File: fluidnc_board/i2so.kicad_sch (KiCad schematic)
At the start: 13 parts

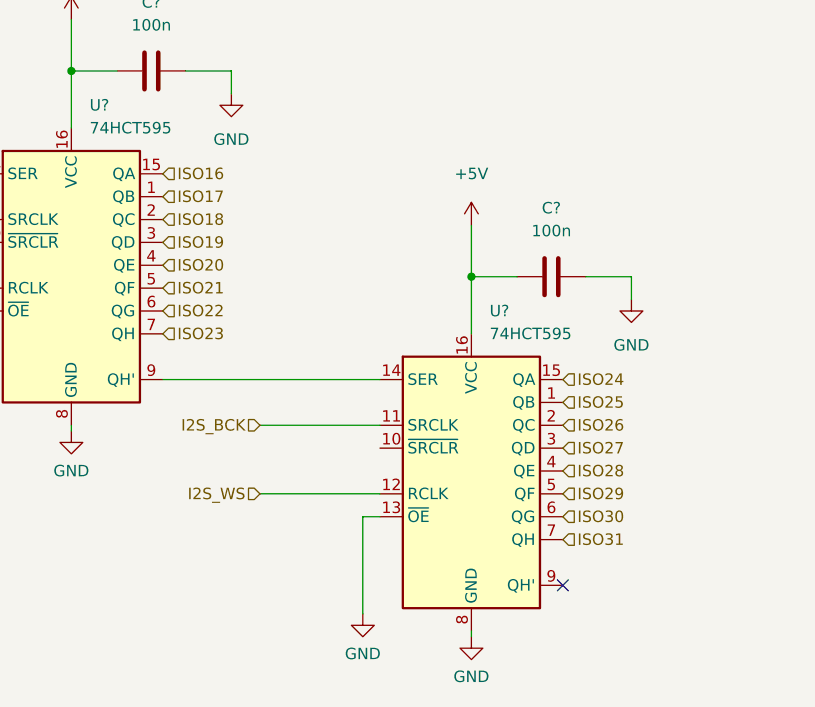
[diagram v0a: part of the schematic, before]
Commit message: remove unnecessary i2s chip
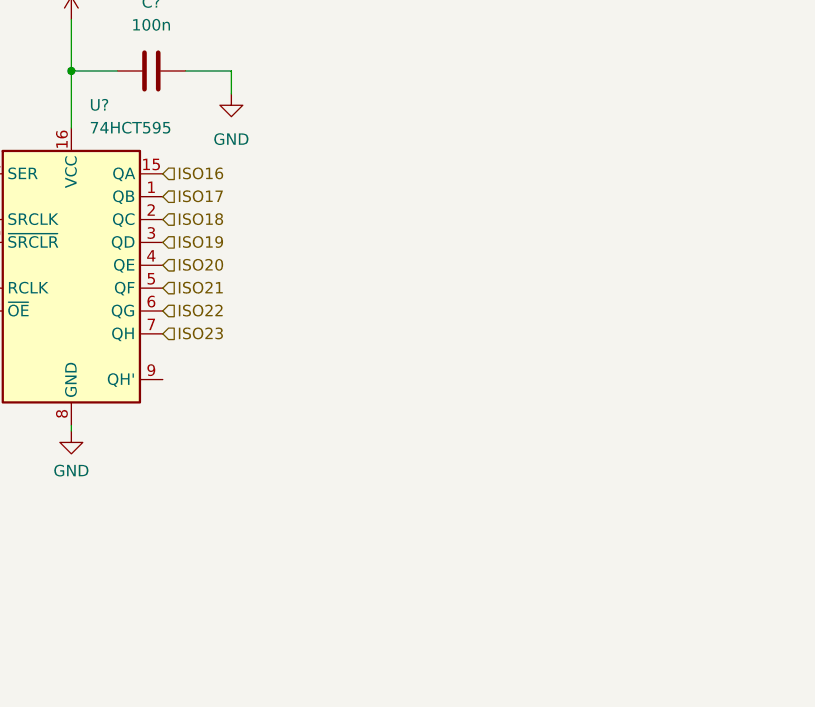
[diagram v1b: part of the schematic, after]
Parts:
- removed C?: 100n, symbol Device:C
- removed U?: 74HCT595, symbol 74xx:74HCT595
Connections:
- no-connect marks 1 -> 0
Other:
- title: (none) -> Outputs Expander
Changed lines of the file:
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@@
 (kicad_sch (version 20211123) (generator eeschema)
   (paper "A4")
+  (title_block
+    (title "Outputs Expander")
+  )
   (junction (at 212.09 68.58) (diameter 0) (color 0 0 0 0)
   )
@@
   (junction (at 62.865 48.895) (diameter 0) (color 0 0 0 0)
   )
-  (junction (at 126.365 142.24) (diameter 0) (color 0 0 0 0)
-  )
   (junction (at 81.915 119.38) (diameter 0) (color 0 0 0 0)
   )
@@
   (junction (at 212.09 79.375) (diameter 0) (color 0 0 0 0)
   )
-  (no_connect (at 136.525 176.53))
   (wire (pts (xy 231.14 68.58) (xy 218.44 68.58))
     (stroke (width 0) (type default) (color 0 0 0 0))
@@
     (stroke (width 0) (type default) (color 0 0 0 0))
   )
-  (wire (pts (xy 114.3 168.91) (xy 116.205 168.91))
-    (stroke (width 0) (type default) (color 0 0 0 0))
-  )
   (wire (pts (xy 231.14 70.485) (xy 231.14 68.58))
     (stroke (width 0) (type default) (color 0 0 0 0))
@@
     (stroke (width 0) (type default) (color 0 0 0 0))
   )
-  (wire (pts (xy 92.075 153.67) (xy 116.205 153.67))
-    (stroke (width 0) (type default) (color 0 0 0 0))
-  )
-  (wire (pts (xy 144.145 142.24) (xy 139.065 142.24))
-    (stroke (width 0) (type default) (color 0 0 0 0))
-  )
   (wire (pts (xy 212.09 66.675) (xy 212.09 68.58))
     (stroke (width 0) (type default) (color 0 0 0 0))
@@
     (stroke (width 0) (type default) (color 0 0 0 0))
   )
-  (wire (pts (xy 126.365 142.24) (xy 126.365 148.59))
-    (stroke (width 0) (type default) (color 0 0 0 0))
-  )
   (wire (pts (xy 81.915 32.385) (xy 81.915 38.735))
     (stroke (width 0) (type default) (color 0 0 0 0))
@@
     (stroke (width 0) (type default) (color 0 0 0 0))
   )
-  (wire (pts (xy 126.365 136.525) (xy 126.365 142.24))
-    (stroke (width 0) (type default) (color 0 0 0 0))
-  )
   (wire (pts (xy 102.87 79.375) (xy 116.205 79.375))
     (stroke (width 0) (type default) (color 0 0 0 0))
@@
     (stroke (width 0) (type default) (color 0 0 0 0))
   )
-  (wire (pts (xy 114.3 168.91) (xy 114.3 179.705))
-    (stroke (width 0) (type default) (color 0 0 0 0))
-  )
-  (wire (pts (xy 102.87 158.75) (xy 116.205 158.75))
-    (stroke (width 0) (type default) (color 0 0 0 0))
-  )
   (wire (pts (xy 58.42 135.89) (xy 71.755 135.89))
     (stroke (width 0) (type default) (color 0 0 0 0))
   )
-  (wire (pts (xy 126.365 181.61) (xy 126.365 182.245))
-    (stroke (width 0) (type default) (color 0 0 0 0))
-  )
   (wire (pts (xy 212.09 79.375) (xy 205.105 79.375))
     (stroke (width 0) (type default) (color 0 0 0 0))
@@
     (stroke (width 0) (type default) (color 0 0 0 0))
   )
-  (wire (pts (xy 144.145 144.78) (xy 144.145 142.24))
-    (stroke (width 0) (type default) (color 0 0 0 0))
-  )
   (wire (pts (xy 81.915 71.755) (xy 81.915 72.39))
     (stroke (width 0) (type default) (color 0 0 0 0))
@@
   )
   (wire (pts (xy 231.14 78.105) (xy 231.14 79.375))
-    (stroke (width 0) (type default) (color 0 0 0 0))
-  )
-  (wire (pts (xy 102.87 166.37) (xy 116.205 166.37))
-    (stroke (width 0) (type default) (color 0 0 0 0))
-  )
-  (wire (pts (xy 126.365 142.24) (xy 131.445 142.24))
     (stroke (width 0) (type default) (color 0 0 0 0))
   )
@@
     (effects (font (size 1.27 1.27)) (justify right))
   )
-  (hierarchical_label "ISO26" (shape input) (at 136.525 158.75 0)
-    (effects (font (size 1.27 1.27)) (justify left))
-  )
   (hierarchical_label "ISO7" (shape input) (at 92.075 61.595 0)
     (effects (font (size 1.27 1.27)) (justify left))
@@
     (effects (font (size 1.27 1.27)) (justify left))
   )
-  (hierarchical_label "ISO31" (shape input) (at 136.525 171.45 0)
-    (effects (font (size 1.27 1.27)) (justify left))
-  )
   (hierarchical_label "ISO2" (shape input) (at 92.075 48.895 0)
     (effects (font (size 1.27 1.27)) (justify left))
@@
     (effects (font (size 1.27 1.27)) (justify left))
   )
-  (hierarchical_label "ISO29" (shape input) (at 136.525 166.37 0)
-    (effects (font (size 1.27 1.27)) (justify left))
-  )
-  (hierarchical_label "ISO25" (shape input) (at 136.525 156.21 0)
-    (effects (font (size 1.27 1.27)) (justify left))
-  )
-  (hierarchical_label "ISO24" (shape input) (at 136.525 153.67 0)
-    (effects (font (size 1.27 1.27)) (justify left))
-  )
   (hierarchical_label "ISO13" (shape input) (at 136.525 79.375 0)
-    (effects (font (size 1.27 1.27)) (justify left))
-  )
-  (hierarchical_label "ISO27" (shape input) (at 136.525 161.29 0)
     (effects (font (size 1.27 1.27)) (justify left))
   )
@@
     (effects (font (size 1.27 1.27)) (justify left))
   )
-  (hierarchical_label "I2S_BCK" (shape input) (at 102.87 158.75 180)
-    (effects (font (size 1.27 1.27)) (justify right))
-  )
   (hierarchical_label "I2S_DATA" (shape input) (at 58.42 43.815 180)
     (effects (font (size 1.27 1.27)) (justify right))
   )
-  (hierarchical_label "ISO30" (shape input) (at 136.525 168.91 0)
-    (effects (font (size 1.27 1.27)) (justify left))
-  )
   (hierarchical_label "ISO22" (shape input) (at 92.075 146.05 0)
     (effects (font (size 1.27 1.27)) (justify left))
   )
   (hierarchical_label "ISO21" (shape input) (at 92.075 143.51 0)
-    (effects (font (size 1.27 1.27)) (justify left))
-  )
-  (hierarchical_label "I2S_WS" (shape input) (at 102.87 166.37 180)
-    (effects (font (size 1.27 1.27)) (justify right))
-  )
-  (hierarchical_label "ISO28" (shape input) (at 136.525 163.83 0)
     (effects (font (size 1.27 1.27)) (justify left))
   )
@@
     (pin "9")
   )
-  (symbol (lib_id "power:+5V") (at 126.365 136.525 0) (unit 1)
-    (in_bom yes) (on_board yes) (fields_autoplaced)
-    (property "Reference" "#PWR?" (id 0) (at 126.365 140.335 0)
-      (effects (font (size 1.27 1.27)) hide)
-    )
-    (property "Value" "+5V" (id 1) (at 126.365 130.81 0))
-    (property "Footprint" "" (id 2) (at 126.365 136.525 0)
-      (effects (font (size 1.27 1.27)) hide)
-    )
-    (property "Datasheet" "" (id 3) (at 126.365 136.525 0)
-      (effects (font (size 1.27 1.27)) hide)
-    )
-    (pin "1")
-  )
   (symbol (lib_id "Device:C") (at 135.255 55.245 90) (unit 1)
     (in_bom yes) (on_board yes) (fields_autoplaced)
@@
     (pin "2")
   )
-  (symbol (lib_id "Device:C") (at 135.255 142.24 90) (unit 1)
-    (in_bom yes) (on_board yes) (fields_autoplaced)
-    (property "Reference" "C?" (id 0) (at 135.255 134.62 90))
-    (property "Value" "100n" (id 1) (at 135.255 137.16 90))
-    (property "Footprint" "" (id 2) (at 139.065 141.2748 0)
-      (effects (font (size 1.27 1.27)) hide)
-    )
-    (property "Datasheet" "~" (id 3) (at 135.255 142.24 0)
-      (effects (font (size 1.27 1.27)) hide)
-    )
-    (pin "1")
-    (pin "2")
-  )
   (symbol (lib_id "Device:C") (at 191.77 74.295 0) (unit 1)
     (in_bom yes) (on_board yes) (fields_autoplaced)
@@
     (pin "1")
     (pin "2")
-  )
-  (symbol (lib_id "power:GND") (at 126.365 182.245 0) (unit 1)
-    (in_bom yes) (on_board yes) (fields_autoplaced)
-    (property "Reference" "#PWR?" (id 0) (at 126.365 188.595 0)
-      (effects (font (size 1.27 1.27)) hide)
-    )
-    (property "Value" "GND" (id 1) (at 126.365 186.69 0))
-    (property "Footprint" "" (id 2) (at 126.365 182.245 0)
-      (effects (font (size 1.27 1.27)) hide)
-    )
-    (property "Datasheet" "" (id 3) (at 126.365 182.245 0)
-      (effects (font (size 1.27 1.27)) hide)
-    )
-    (pin "1")
-  )
-  (symbol (lib_id "power:GND") (at 144.145 144.78 0) (unit 1)
-    (in_bom yes) (on_board yes) (fields_autoplaced)
-    (property "Reference" "#PWR?" (id 0) (at 144.145 151.13 0)
-      (effects (font (size 1.27 1.27)) hide)
-    )
-    (property "Value" "GND" (id 1) (at 144.145 149.86 0))
-    (property "Footprint" "" (id 2) (at 144.145 144.78 0)
-      (effects (font (size 1.27 1.27)) hide)
-    )
-    (property "Datasheet" "" (id 3) (at 144.145 144.78 0)
-      (effects (font (size 1.27 1.27)) hide)
-    )
-    (pin "1")
   )
   (symbol (lib_id "power:GND") (at 99.695 34.925 0) (unit 1)
@@
     (pin "1")
   )
-  (symbol (lib_id "74xx:74HCT595") (at 126.365 163.83 0) (unit 1)
-    (in_bom yes) (on_board yes) (fields_autoplaced)
-    (property "Reference" "U?" (id 0) (at 128.3844 146.05 0)
-      (effects (font (size 1.27 1.27)) (justify left))
-    )
-    (property "Value" "74HCT595" (id 1) (at 128.3844 148.59 0)
-      (effects (font (size 1.27 1.27)) (justify left))
-    )
-    (property "Footprint" "" (id 2) (at 126.365 163.83 0)
-      (effects (font (size 1.27 1.27)) hide)
-    )
-    (property "Datasheet" "https://assets.nexperia.com/documents/data-sheet/74HC_HCT595.pdf" (id 3) (at 126.365 163.83 0)
-      (effects (font (size 1.27 1.27)) hide)
-    )
-    (pin "1")
-    (pin "10")
-    (pin "11")
-    (pin "12")
-    (pin "13")
-    (pin "14")
-    (pin "15")
-    (pin "16")
-    (pin "2")
-    (pin "3")
-    (pin "4")
-    (pin "5")
-    (pin "6")
-    (pin "7")
-    (pin "8")
-    (pin "9")
-  )
   (symbol (lib_id "Device:C") (at 218.44 74.295 0) (unit 1)
     (in_bom yes) (on_board yes) (fields_autoplaced)
@@
     (pin "2")
   )
-  (symbol (lib_id "power:GND") (at 114.3 179.705 0) (unit 1)
-    (in_bom yes) (on_board yes) (fields_autoplaced)
-    (property "Reference" "#PWR?" (id 0) (at 114.3 186.055 0)
-      (effects (font (size 1.27 1.27)) hide)
-    )
-    (property "Value" "GND" (id 1) (at 114.3 184.15 0))
-    (property "Footprint" "" (id 2) (at 114.3 179.705 0)
-      (effects (font (size 1.27 1.27)) hide)
-    )
-    (property "Datasheet" "" (id 3) (at 114.3 179.705 0)
-      (effects (font (size 1.27 1.27)) hide)
-    )
-    (pin "1")
-  )
   (symbol (lib_id "power:GND") (at 144.145 57.785 0) (unit 1)

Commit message: footprint associations and part no.
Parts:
- C63, C64, C65, C66, C67, C68, C69: renamed from C?; footprint (none) -> Capacitor_SMD:C_0603_1608Metric_Pad1.05x0.95mm_HandSolder; Digikey Part No. (none) -> 1276-1941-1-ND
- R50: renamed from R?; footprint (none) -> Resistor_SMD:R_0805_2012Metric_Pad1.20x1.40mm_HandSolder; Digikey Part No. (none) -> 311-10KARCT-ND
- U20, U21, U22: renamed from U?; footprint (none) -> Package_SO:TSSOP-16_4.4x5mm_P0.65mm; Digikey Part No. (none) -> MC74HCT595ADTGOS-ND

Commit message: fixed some footprint associations, placed footprints
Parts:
- C63, C64, C65, C66, C67, C68, C69: footprint Capacitor_SMD:C_0603_1608Metric_Pad1.05x0.95mm_HandSolder -> Capacitor_SMD:C_0603_1608Metric_Pad1.08x0.95mm_HandSolder; Digikey Part No. 1276-1941-1-ND -> (none)
- R50: Digikey Part No. 311-10KARCT-ND -> (none)
- U20, U21, U22: Digikey Part No. MC74HCT595ADTGOS-ND -> (none)
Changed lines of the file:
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@@
-      (effects (font (size 1.27 1.27)) hide)
-    )
-    (property "Digikey Part No." "MC74HCT595ADTGOS-ND" (id 4) (at 126.365 76.835 0)
       (effects (font (size 1.27 1.27)) hide)
     )
@@
     (property "Reference" "C63" (id 0) (at 90.805 24.765 90))
     (property "Value" "100n" (id 1) (at 90.805 27.305 90))
-    (property "Footprint" "Capacitor_SMD:C_0603_1608Metric_Pad1.05x0.95mm_HandSolder" (id 2) (at 94.615 31.4198 0)
-      (effects (font (size 1.27 1.27)) hide)
-    )
-    (property "Datasheet" "http://www.samsungsem.com/kr/support/product-search/mlcc/CL10B104MB8NNNC.jsp" (id 3) (at 90.805 32.385 0)
-      (effects (font (size 1.27 1.27)) hide)
-    )
-    (property "Digikey Part No." "1276-1941-1-ND" (id 4) (at 90.805 32.385 0)
+    (property "Footprint" "Capacitor_SMD:C_0603_1608Metric_Pad1.08x0.95mm_HandSolder" (id 2) (at 94.615 31.4198 0)
+      (effects (font (size 1.27 1.27)) hide)
+    )
+    (property "Datasheet" "~" (id 3) (at 90.805 32.385 0)
       (effects (font (size 1.27 1.27)) hide)
     )
@@
     )
     (property "Datasheet" "https://assets.nexperia.com/documents/data-sheet/74HC_HCT595.pdf" (id 3) (at 81.915 53.975 0)
-      (effects (font (size 1.27 1.27)) hide)
-    )
-    (property "Digikey Part No." "MC74HCT595ADTGOS-ND" (id 4) (at 81.915 53.975 0)
       (effects (font (size 1.27 1.27)) hide)
     )
@@
     (property "Reference" "C65" (id 0) (at 135.255 47.625 90))
     (property "Value" "100n" (id 1) (at 135.255 50.165 90))
-    (property "Footprint" "Capacitor_SMD:C_0603_1608Metric_Pad1.05x0.95mm_HandSolder" (id 2) (at 139.065 54.2798 0)
-      (effects (font (size 1.27 1.27)) hide)
-    )
-    (property "Datasheet" "http://www.samsungsem.com/kr/support/product-search/mlcc/CL10B104MB8NNNC.jsp" (id 3) (at 135.255 55.245 0)
-      (effects (font (size 1.27 1.27)) hide)
-    )
-    (property "Digikey Part No." "1276-1941-1-ND" (id 4) (at 135.255 55.245 0)
+    (property "Footprint" "Capacitor_SMD:C_0603_1608Metric_Pad1.08x0.95mm_HandSolder" (id 2) (at 139.065 54.2798 0)
+      (effects (font (size 1.27 1.27)) hide)
+    )
+    (property "Datasheet" "~" (id 3) (at 135.255 55.245 0)
       (effects (font (size 1.27 1.27)) hide)
     )
@@
     )
     (property "Datasheet" "https://assets.nexperia.com/documents/data-sheet/74HC_HCT595.pdf" (id 3) (at 81.915 140.97 0)
-      (effects (font (size 1.27 1.27)) hide)
-    )
-    (property "Digikey Part No." "MC74HCT595ADTGOS-ND" (id 4) (at 81.915 140.97 0)
       (effects (font (size 1.27 1.27)) hide)
     )
@@
       (effects (font (size 1.27 1.27)) (justify left))
     )
-    (property "Footprint" "Capacitor_SMD:C_0603_1608Metric_Pad1.05x0.95mm_HandSolder" (id 2) (at 232.1052 78.105 0)
-      (effects (font (size 1.27 1.27)) hide)
-    )
-    (property "Datasheet" "http://www.samsungsem.com/kr/support/product-search/mlcc/CL10B104MB8NNNC.jsp" (id 3) (at 231.14 74.295 0)
-      (effects (font (size 1.27 1.27)) hide)
-    )
-    (property "Digikey Part No." "1276-1941-1-ND" (id 4) (at 231.14 74.295 0)
+    (property "Footprint" "Capacitor_SMD:C_0603_1608Metric_Pad1.08x0.95mm_HandSolder" (id 2) (at 232.1052 78.105 0)
+      (effects (font (size 1.27 1.27)) hide)
+    )
+    (property "Datasheet" "~" (id 3) (at 231.14 74.295 0)
       (effects (font (size 1.27 1.27)) hide)
     )
@@
       (effects (font (size 1.27 1.27)) hide)
     )
-    (property "Datasheet" "https://www.yageo.com/upload/media/product/productsearch/datasheet/rchip/PYu-RC_Group_51_RoHS_L_11.pdf" (id 3) (at 62.865 64.77 0)
-      (effects (font (size 1.27 1.27)) hide)
-    )
-    (property "Digikey Part No." "311-10KARCT-ND" (id 4) (at 62.865 64.77 0)
+    (property "Datasheet" "~" (id 3) (at 62.865 64.77 0)
       (effects (font (size 1.27 1.27)) hide)
     )
@@
       (effects (font (size 1.27 1.27)) (justify left))
     )
-    (property "Footprint" "Capacitor_SMD:C_0603_1608Metric_Pad1.05x0.95mm_HandSolder" (id 2) (at 192.7352 78.105 0)
-      (effects (font (size 1.27 1.27)) hide)
-    )
-    (property "Datasheet" "http://www.samsungsem.com/kr/support/product-search/mlcc/CL10B104MB8NNNC.jsp" (id 3) (at 191.77 74.295 0)
-      (effects (font (size 1.27 1.27)) hide)
-    )
-    (property "Digikey Part No." "1276-1941-1-ND" (id 4) (at 191.77 74.295 0)
+    (property "Footprint" "Capacitor_SMD:C_0603_1608Metric_Pad1.08x0.95mm_HandSolder" (id 2) (at 192.7352 78.105 0)
+      (effects (font (size 1.27 1.27)) hide)
+    )
+    (property "Datasheet" "~" (id 3) (at 191.77 74.295 0)
       (effects (font (size 1.27 1.27)) hide)
     )
@@
       (effects (font (size 1.27 1.27)) (justify left))
     )
-    (property "Footprint" "Capacitor_SMD:C_0603_1608Metric_Pad1.05x0.95mm_HandSolder" (id 2) (at 219.4052 78.105 0)
-      (effects (font (size 1.27 1.27)) hide)
-    )
-    (property "Datasheet" "http://www.samsungsem.com/kr/support/product-search/mlcc/CL10B104MB8NNNC.jsp" (id 3) (at 218.44 74.295 0)
-      (effects (font (size 1.27 1.27)) hide)
-    )
-    (property "Digikey Part No." "1276-1941-1-ND" (id 4) (at 218.44 74.295 0)
+    (property "Footprint" "Capacitor_SMD:C_0603_1608Metric_Pad1.08x0.95mm_HandSolder" (id 2) (at 219.4052 78.105 0)
+      (effects (font (size 1.27 1.27)) hide)
+    )
+    (property "Datasheet" "~" (id 3) (at 218.44 74.295 0)
       (effects (font (size 1.27 1.27)) hide)
     )
@@
       (effects (font (size 1.27 1.27)) (justify left))
     )
-    (property "Footprint" "Capacitor_SMD:C_0603_1608Metric_Pad1.05x0.95mm_HandSolder" (id 2) (at 206.0702 78.105 0)
-      (effects (font (size 1.27 1.27)) hide)
-    )
-    (property "Datasheet" "http://www.samsungsem.com/kr/support/product-search/mlcc/CL10B104MB8NNNC.jsp" (id 3) (at 205.105 74.295 0)
-      (effects (font (size 1.27 1.27)) hide)
-    )
-    (property "Digikey Part No." "1276-1941-1-ND" (id 4) (at 205.105 74.295 0)
+    (property "Footprint" "Capacitor_SMD:C_0603_1608Metric_Pad1.08x0.95mm_HandSolder" (id 2) (at 206.0702 78.105 0)
+      (effects (font (size 1.27 1.27)) hide)
+    )
+    (property "Datasheet" "~" (id 3) (at 205.105 74.295 0)
       (effects (font (size 1.27 1.27)) hide)
     )
@@
     (property "Reference" "C64" (id 0) (at 90.805 111.76 90))
     (property "Value" "100n" (id 1) (at 90.805 114.3 90))
-    (property "Footprint" "Capacitor_SMD:C_0603_1608Metric_Pad1.05x0.95mm_HandSolder" (id 2) (at 94.615 118.4148 0)
-      (effects (font (size 1.27 1.27)) hide)
-    )
-    (property "Datasheet" "http://www.samsungsem.com/kr/support/product-search/mlcc/CL10B104MB8NNNC.jsp" (id 3) (at 90.805 119.38 0)
-      (effects (font (size 1.27 1.27)) hide)
-    )
-    (property "Digikey Part No." "1276-1941-1-ND" (id 4) (at 90.805 119.38 0)
-      (effects (font (size 1.27 1.27)) hide)
-    )
+    (property "Footprint" "Capacitor_SMD:C_0603_1608Metric_Pad1.08x0.95mm_HandSolder" (id 2) (at 94.615 118.4148 0)
+      (effects (font (size 1.27 1.27)) hide)
+    )
+    (property "Datasheet" "~" (id 3) (at 90.805 119.38 0)
+      (effects (font (size 1.27 1.27)) hide)
+    )
